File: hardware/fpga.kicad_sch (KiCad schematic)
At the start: 53 parts, among them J10 Conn_01x03_Pin, J11 Conn_01x03_Pin, J12 Conn_01x10_Pin, J14 Conn_01x03_Pin, J15 Conn_01x02_Pin, J16 Conn_01x03_Pin, U1 ICE40HX4K-TQ144, U2 74HC244

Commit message: route mcu
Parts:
- added C149: 100n, Capacitor_SMD:C_0402_1005Metric, symbol Device:C
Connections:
- net +1V2: now also C149.1
- net GND: now also C149.2
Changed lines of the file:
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@@
 	)
 	(junction
+		(at 73.66 133.35)
+		(diameter 0)
+		(color 0 0 0 0)
+	)
+	(junction
 		(at 248.92 24.13)
 		(diameter 0)
@@
 	)
 	(junction
+		(at 68.58 123.19)
+		(diameter 0)
+		(color 0 0 0 0)
+	)
+	(junction
 		(at 93.98 153.67)
 		(diameter 0)
@@
 		)
 	)
+	(wire
+		(pts
+			(xy 68.58 123.19) (xy 68.58 124.46)
+		)
+		(stroke
+			(width 0)
+			(type default)
+		)
+	)
 	(bus
 		(pts
@@
 		)
 	)
+	(wire
+		(pts
+			(xy 68.58 133.35) (xy 73.66 133.35)
+		)
+		(stroke
+			(width 0)
+			(type default)
+		)
+	)
 	(bus
 		(pts
@@
 	(wire
 		(pts
-			(xy 58.42 123.19) (xy 73.66 123.19)
+			(xy 58.42 123.19) (xy 68.58 123.19)
 		)
 		(stroke
@@
 		)
 	)
+	(wire
+		(pts
+			(xy 68.58 123.19) (xy 73.66 123.19)
+		)
+		(stroke
+			(width 0)
+			(type default)
+		)
+	)
 	(bus
 		(pts
@@
 	(wire
 		(pts
+			(xy 68.58 132.08) (xy 68.58 133.35)
+		)
+		(stroke
+			(width 0)
+			(type default)
+		)
+	)
+	(wire
+		(pts
 			(xy 93.98 166.37) (xy 93.98 153.67)
 		)
@@
 					(unit 1)
 				)
+			)
+		)
+	)
+	(symbol
+		(lib_id "Device:C")
+		(at 68.58 128.27 0)
+		(unit 1)
+		(exclude_from_sim no)
+		(in_bom yes)
+		(on_board yes)
+		(dnp no)
+		(property "Reference" "C149"
+			(at 68.58 124.46 0)
+			(effects
+				(font
+					(size 1.27 1.27)
+				)
+				(justify left)
+			)
+		)
+		(property "Value" "100n"
+			(at 68.58 126.2379 0)
+			(effects
+				(font
+					(size 1.27 1.27)
+				)
+				(justify left)
+			)
+		)
+		(property "Footprint" "Capacitor_SMD:C_0402_1005Metric"
+			(at 69.5452 132.08 0)
+			(effects
+				(font
+					(size 1.27 1.27)
+				)
+				(hide yes)
+			)
+		)
+		(property "Datasheet" "~"
+			(at 68.58 128.27 0)
+			(effects
+				(font
+					(size 1.27 1.27)
+				)
+				(hide yes)
+			)
+		)
+		(property "Description" "Unpolarized capacitor"
+			(at 68.58 128.27 0)
+			(effects
+				(font
+					(size 1.27 1.27)
+				)
+				(hide yes)
+			)
+		)
+		(property "LCSC" "C307331"
+			(at 68.58 128.27 0)
+			(effects
+				(font
+					(size 1.27 1.27)
+				)
+				(hide yes)
+			)
+		)
+		(pin "1"
+		)
+		(pin "2"
+		)
+		(instances
+			(project "digital"
+				(path "/4c5c7ce5-09d6-4a32-b2a0-f32b0c47f27d/5a0bf45b-8051-4130-a070-b09b8e450297"
+					(reference "C149")
+					(unit 1)
+				)

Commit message: wire until sipm power
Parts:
- R20: footprint Resistor_SMD:R_0603_1608Metric -> Resistor_SMD:R_0402_1005Metric; LCSC C21189 -> (none)
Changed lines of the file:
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@@
 			)
 		)
-		(property "Footprint" "Resistor_SMD:R_0603_1608Metric"
+		(property "Footprint" "Resistor_SMD:R_0402_1005Metric"
 			(at 90.678 172.72 90)
 			(effects
@@
 			)
 		)
-		(property "LCSC" "C21189"
+		(property "LCSC" ""
 			(at 88.9 172.72 0)
 			(effects

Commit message: route
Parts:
- renumbered C6 to C10, C7 to C11, C149 to C12, C8 to C13, C10 to C14, C11 to C15, C13 to C16, C14 to C17, C15 to C18, C16 to C19, C17 to C20, C18 to C21, C19 to C22, C20 to C23, C148 to C3, C3 to C4, C147 to C5, C4 to C6, C12 to C7, C5 to C8, J14 to J13, J15 to J14, J16 to J15, TP43 to TP1, TP44 to TP2, TP1 to TP3
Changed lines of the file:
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@@
 		(on_board yes)
 		(dnp no)
-		(property "Reference" "C13"
+		(property "Reference" "C16"
 			(at 88.9 124.46 0)
 			(effects
@@
 			(project "digital"
 				(path "/4c5c7ce5-09d6-4a32-b2a0-f32b0c47f27d/5a0bf45b-8051-4130-a070-b09b8e450297"
-					(reference "C13")
+					(reference "C16")
 					(unit 1)
 				)
@@
 		(on_board yes)
 		(dnp no)
-		(property "Reference" "C18"
+		(property "Reference" "C21"
 			(at 80.01 144.78 0)
 			(effects
@@
 			(project "digital"
 				(path "/4c5c7ce5-09d6-4a32-b2a0-f32b0c47f27d/5a0bf45b-8051-4130-a070-b09b8e450297"
-					(reference "C18")
+					(reference "C21")
 					(unit 1)
 				)
@@
 		(on_board yes)
 		(dnp no)
-		(property "Reference" "C10"
+		(property "Reference" "C14"
 			(at 78.74 124.46 0)
 			(effects
@@
 			(project "digital"
 				(path "/4c5c7ce5-09d6-4a32-b2a0-f32b0c47f27d/5a0bf45b-8051-4130-a070-b09b8e450297"
-					(reference "C10")
+					(reference "C14")
 					(unit 1)
 				)
@@
 		(on_board yes)
 		(dnp no)
-		(property "Reference" "C14"
+		(property "Reference" "C17"
 			(at 35.306 129.286 90)
 			(effects
@@
 			(project "digital"
 				(path "/4c5c7ce5-09d6-4a32-b2a0-f32b0c47f27d/5a0bf45b-8051-4130-a070-b09b8e450297"
-					(reference "C14")
+					(reference "C17")
 					(unit 1)
 				)
@@
 		(on_board yes)
 		(dnp no)
-		(property "Reference" "C20"
+		(property "Reference" "C23"
 			(at 93.98 144.78 0)
 			(effects
@@
 			(project "digital"
 				(path "/4c5c7ce5-09d6-4a32-b2a0-f32b0c47f27d/5a0bf45b-8051-4130-a070-b09b8e450297"
-					(reference "C20")
+					(reference "C23")
 					(unit 1)
 				)
@@
 		(on_board yes)
 		(dnp no)
-		(property "Reference" "C147"
+		(property "Reference" "C5"
 			(at 140.97 25.4 0)
 			(effects
@@
 			(project "digital"
 				(path "/4c5c7ce5-09d6-4a32-b2a0-f32b0c47f27d/5a0bf45b-8051-4130-a070-b09b8e450297"
-					(reference "C147")
+					(reference "C5")
 					(unit 1)
 				)
@@
 		(on_board yes)
 		(dnp no)
-		(property "Reference" "TP1"
+		(property "Reference" "TP3"
 			(at 41.402 109.982 90)
 			(effects
@@
 			(project "digital"
 				(path "/4c5c7ce5-09d6-4a32-b2a0-f32b0c47f27d/5a0bf45b-8051-4130-a070-b09b8e450297"
-					(reference "TP1")
+					(reference "TP3")
 					(unit 1)
 				)
@@
 		(on_board yes)
 		(dnp no)
-		(property "Reference" "C8"
+		(property "Reference" "C13"
 			(at 73.66 124.46 0)
 			(effects
@@
 			(project "digital"
 				(path "/4c5c7ce5-09d6-4a32-b2a0-f32b0c47f27d/5a0bf45b-8051-4130-a070-b09b8e450297"
-					(reference "C8")
+					(reference "C13")
 					(unit 1)
 				)
@@
 		(on_board yes)
 		(dnp no)
-		(property "Reference" "J16"
+		(property "Reference" "J15"
 			(at 96.266 90.678 0)
 			(effects
@@
 			(project "digital"
 				(path "/4c5c7ce5-09d6-4a32-b2a0-f32b0c47f27d/5a0bf45b-8051-4130-a070-b09b8e450297"
-					(reference "J16")
+					(reference "J15")
 					(unit 1)
 				)
@@
 		(on_board yes)
 		(dnp no)
-		(property "Reference" "C15"
+		(property "Reference" "C18"
 			(at 35.306 134.366 90)
 			(effects
@@
 			(project "digital"
 				(path "/4c5c7ce5-09d6-4a32-b2a0-f32b0c47f27d/5a0bf45b-8051-4130-a070-b09b8e450297"
-					(reference "C15")
+					(reference "C18")
 					(unit 1)
 				)
@@
 		(on_board yes)
 		(dnp no)
-		(property "Reference" "C11"
+		(property "Reference" "C15"
 			(at 83.82 124.46 0)
 			(effects
@@
 			(project "digital"
 				(path "/4c5c7ce5-09d6-4a32-b2a0-f32b0c47f27d/5a0bf45b-8051-4130-a070-b09b8e450297"
-					(reference "C11")
+					(reference "C15")
 					(unit 1)
 				)
@@
 		(on_board yes)
 		(dnp no)
-		(property "Reference" "C7"
+		(property "Reference" "C11"
 			(at 158.496 110.236 90)
 			(effects
@@
 			(project "digital"
 				(path "/4c5c7ce5-09d6-4a32-b2a0-f32b0c47f27d/5a0bf45b-8051-4130-a070-b09b8e450297"
-					(reference "C7")
+					(reference "C11")
 					(unit 1)
 				)
@@
 		(on_board yes)
 		(dnp no)
-		(property "Reference" "C3"
+		(property "Reference" "C4"
 			(at 135.89 25.4 0)
 			(effects
@@
 			(project "digital"
 				(path "/4c5c7ce5-09d6-4a32-b2a0-f32b0c47f27d/5a0bf45b-8051-4130-a070-b09b8e450297"
-					(reference "C3")
+					(reference "C4")
 					(unit 1)
 				)
@@
 		(on_board yes)
 		(dnp no)
-		(property "Reference" "J15"
+		(property "Reference" "J14"
 			(at 222.25 82.2959 0)
 			(effects
@@
 			(project "digital"
 				(path "/4c5c7ce5-09d6-4a32-b2a0-f32b0c47f27d/5a0bf45b-8051-4130-a070-b09b8e450297"
-					(reference "J15")
+					(reference "J14")
 					(unit 1)
 				)
@@
 		(on_board yes)
 		(dnp no)
-		(property "Reference" "C149"
+		(property "Reference" "C12"
 			(at 68.58 124.46 0)
 			(effects
@@
 			(project "digital"
 				(path "/4c5c7ce5-09d6-4a32-b2a0-f32b0c47f27d/5a0bf45b-8051-4130-a070-b09b8e450297"
-					(reference "C149")
+					(reference "C12")
 					(unit 1)
 				)
@@
 		(on_board yes)
 		(dnp no)
-		(property "Reference" "J14"
+		(property "Reference" "J13"
 			(at 153.416 80.518 0)
 			(effects
@@
 			(project "digital"
 				(path "/4c5c7ce5-09d6-4a32-b2a0-f32b0c47f27d/5a0bf45b-8051-4130-a070-b09b8e450297"
-					(reference "J14")
+					(reference "J13")
 					(unit 1)
 				)
@@
 		(on_board yes)
 		(dnp no)
-		(property "Reference" "C5"
+		(property "Reference" "C8"
 			(at 259.08 25.4 0)
 			(effects
@@
 			(project "digital"
 				(path "/4c5c7ce5-09d6-4a32-b2a0-f32b0c47f27d/5a0bf45b-8051-4130-a070-b09b8e450297"
-					(reference "C5")
+					(reference "C8")
 					(unit 1)
 				)
@@
 		(on_board yes)
 		(dnp no)
-		(property "Reference" "C19"
+		(property "Reference" "C22"
 			(at 85.09 144.78 0)
 			(effects
@@
 			(project "digital"
 				(path "/4c5c7ce5-09d6-4a32-b2a0-f32b0c47f27d/5a0bf45b-8051-4130-a070-b09b8e450297"
-					(reference "C19")
+					(reference "C22")
 					(unit 1)
 				)
@@
 		(on_board yes)
 		(dnp no)
-		(property "Reference" "TP43"
+		(property "Reference" "TP1"
 			(at 30.48 80.01 90)
 			(effects
@@
 			(project "digital"
 				(path "/4c5c7ce5-09d6-4a32-b2a0-f32b0c47f27d/5a0bf45b-8051-4130-a070-b09b8e450297"
-					(reference "TP43")
+					(reference "TP1")
 					(unit 1)
 				)
@@
 		(on_board yes)
 		(dnp no)
-		(property "Reference" "C4"
+		(property "Reference" "C6"
 			(at 193.04 25.4 0)
 			(effects
@@
 			(project "digital"
 				(path "/4c5c7ce5-09d6-4a32-b2a0-f32b0c47f27d/5a0bf45b-8051-4130-a070-b09b8e450297"
-					(reference "C4")
+					(reference "C6")
 					(unit 1)
 				)
@@
 		(on_board yes)
 		(dnp no)
-		(property "Reference" "TP44"
+		(property "Reference" "TP2"
 			(at 30.48 82.55 90)
 			(effects
@@
 			(project "digital"
 				(path "/4c5c7ce5-09d6-4a32-b2a0-f32b0c47f27d/5a0bf45b-8051-4130-a070-b09b8e450297"
-					(reference "TP44")
+					(reference "TP2")
 					(unit 1)
 				)
@@
 		(on_board yes)
 		(dnp no)
-		(property "Reference" "C12"
+		(property "Reference" "C7"
 			(at 198.12 25.4 0)
 			(effects
@@
 			(project "digital"
 				(path "/4c5c7ce5-09d6-4a32-b2a0-f32b0c47f27d/5a0bf45b-8051-4130-a070-b09b8e450297"
-					(reference "C12")
+					(reference "C7")
 					(unit 1)
 				)
@@
 		(on_board yes)
 		(dnp no)
-		(property "Reference" "C148"
+		(property "Reference" "C3"
 			(at 85.09 25.4 0)
 			(effects
@@
 			(project "digital"
 				(path "/4c5c7ce5-09d6-4a32-b2a0-f32b0c47f27d/5a0bf45b-8051-4130-a070-b09b8e450297"
-					(reference "C148")
+					(reference "C3")
 					(unit 1)
 				)
@@
 		(on_board yes)
 		(dnp no)
-		(property "Reference" "C6"
+		(property "Reference" "C10"
 			(at 156.21 105.664 90)
 			(effects
@@
 			(project "digital"
 				(path "/4c5c7ce5-09d6-4a32-b2a0-f32b0c47f27d/5a0bf45b-8051-4130-a070-b09b8e450297"
-					(reference "C6")
+					(reference "C10")
 					(unit 1)
 				)
@@
 		(on_board yes)
 		(dnp no)
-		(property "Reference" "C17"
+		(property "Reference" "C20"
 			(at 35.306 144.526 90)
 			(effects
@@
 			(project "digital"
 				(path "/4c5c7ce5-09d6-4a32-b2a0-f32b0c47f27d/5a0bf45b-8051-4130-a070-b09b8e450297"
-					(reference "C17")
+					(reference "C20")
 					(unit 1)
 				)
@@
 		(on_board yes)
 		(dnp no)
-		(property "Reference" "C16"
+		(property "Reference" "C19"
 			(at 35.306 139.446 90)
 			(effects
@@
 			(project "digital"
 				(path "/4c5c7ce5-09d6-4a32-b2a0-f32b0c47f27d/5a0bf45b-8051-4130-a070-b09b8e450297"
-					(reference "C16")
+					(reference "C19")
 					(unit 1)
 				)

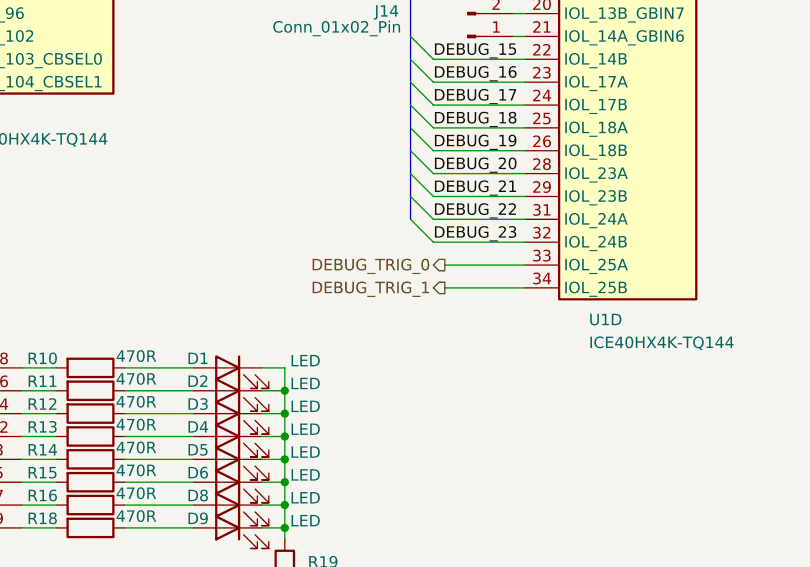
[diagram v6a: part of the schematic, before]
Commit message: route all signal
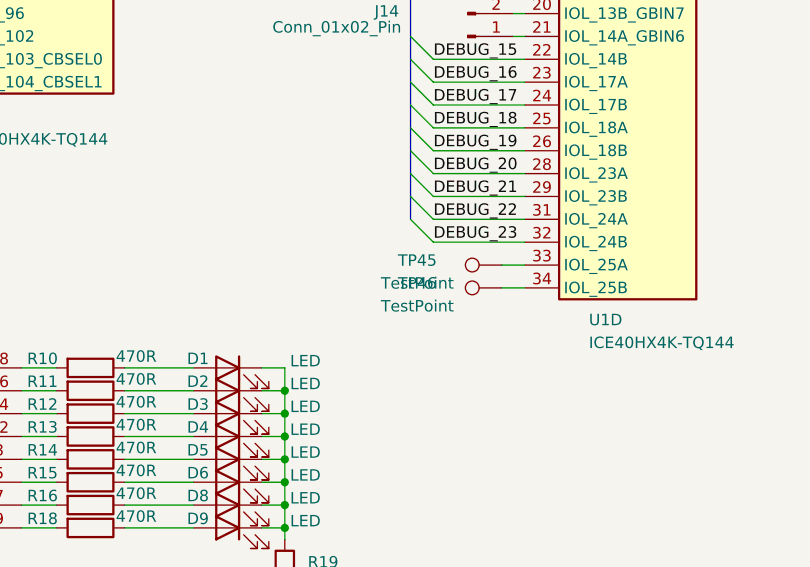
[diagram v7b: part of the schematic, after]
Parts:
- added TP45, TP46: TestPoint, TestPoint:TestPoint_Pad_D1.0mm, symbol Connector:TestPoint
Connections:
- net DEBUG_TRIG_0: no longer names the net of U1.33 (IOL_25A)
- net DEBUG_TRIG_0: now also TP45.1
- net DEBUG_TRIG_1: no longer names the net of U1.34 (IOL_25B)
- net DEBUG_TRIG_1: now also TP46.1
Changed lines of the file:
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@@
 	(wire
 		(pts
+			(xy 233.68 110.49) (xy 236.22 110.49)
+		)
+		(stroke
+			(width 0)
+			(type default)
+		)
+	)
+	(wire
+		(pts
 			(xy 259.08 34.29) (xy 259.08 35.56)
 		)
@@
 	(wire
 		(pts
-			(xy 227.33 113.03) (xy 236.22 113.03)
-		)
-		(stroke
-			(width 0)
-			(type default)
-		)
-	)
-	(wire
-		(pts
 			(xy 76.2 165.1) (xy 78.74 165.1)
 		)
@@
 		)
 	)
+	(wire
+		(pts
+			(xy 233.68 113.03) (xy 236.22 113.03)
+		)
+		(stroke
+			(width 0)
+			(type default)
+		)
+	)
 	(bus
 		(pts
@@
 	(wire
 		(pts
-			(xy 227.33 110.49) (xy 236.22 110.49)
-		)
-		(stroke
-			(width 0)
-			(type default)
-		)
-	)
-	(wire
-		(pts
 			(xy 259.08 24.13) (xy 248.92 24.13)
 		)
@@
 		)
 	)
-	(hierarchical_label "DEBUG_TRIG_1"
-		(shape output)
-		(at 227.33 113.03 180)
-		(effects
-			(font
-				(size 1.27 1.27)
-			)
-			(justify right)
-		)
-	)
 	(hierarchical_label "CDONE"
 		(shape output)
@@
 		)
 	)
-	(hierarchical_label "DEBUG_TRIG_0"
-		(shape output)
-		(at 227.33 110.49 180)
-		(effects
-			(font
-				(size 1.27 1.27)
-			)
-			(justify right)
-		)
-	)
 	(symbol
 		(lib_id "Device:R")
@@
 	)
 	(symbol
+		(lib_id "Connector:TestPoint")
+		(at 233.68 110.49 90)
+		(mirror x)
+		(unit 1)
+		(exclude_from_sim no)
+		(in_bom yes)
+		(on_board yes)
+		(dnp no)
+		(property "Reference" "TP45"
+			(at 224.282 109.982 90)
+			(effects
+				(font
+					(size 1.27 1.27)
+				)
+			)
+		)
+		(property "Value" "TestPoint"
+			(at 224.282 112.522 90)
+			(effects
+				(font
+					(size 1.27 1.27)
+				)
+			)
+		)
+		(property "Footprint" "TestPoint:TestPoint_Pad_D1.0mm"
+			(at 233.68 115.57 0)
+			(effects
+				(font
+					(size 1.27 1.27)
+				)
+				(hide yes)
+			)
+		)
+		(property "Datasheet" "~"
+			(at 233.68 115.57 0)
+			(effects
+				(font
+					(size 1.27 1.27)
+				)
+				(hide yes)
+			)
+		)
+		(property "Description" "test point"
+			(at 233.68 110.49 0)
+			(effects
+				(font
+					(size 1.27 1.27)
+				)
+				(hide yes)
+			)
+		)
+		(pin "1"
+		)
+		(instances
+			(project "digital"
+				(path "/4c5c7ce5-09d6-4a32-b2a0-f32b0c47f27d/5a0bf45b-8051-4130-a070-b09b8e450297"
+					(reference "TP45")
+					(unit 1)
+				)
+			)
+		)
+	)
+	(symbol
 		(lib_id "Device:R")
 		(at 187.96 121.92 270)
@@
 					(unit 1)
 				)
+			)
+		)
+	)
+	(symbol
+		(lib_id "Connector:TestPoint")
+		(at 233.68 113.03 90)
+		(mirror x)
+		(unit 1)
+		(exclude_from_sim no)
+		(in_bom yes)
+		(on_board yes)
+		(dnp no)
+		(property "Reference" "TP46"
+			(at 224.282 112.522 90)
+			(effects
+				(font
+					(size 1.27 1.27)
+				)
+			)
+		)
+		(property "Value" "TestPoint"
+			(at 224.282 115.062 90)
+			(effects
+				(font
+					(size 1.27 1.27)
+				)
+			)
+		)
+		(property "Footprint" "TestPoint:TestPoint_Pad_D1.0mm"
+			(at 233.68 118.11 0)
+			(effects
+				(font
+					(size 1.27 1.27)
+				)
+				(hide yes)
+			)
+		)
+		(property "Datasheet" "~"
+			(at 233.68 118.11 0)
+			(effects
+				(font
+					(size 1.27 1.27)
+				)
+				(hide yes)
+			)
+		)
+		(property "Description" "test point"
+			(at 233.68 113.03 0)
+			(effects
+				(font
+					(size 1.27 1.27)
+				)
+				(hide yes)
+			)
+		)
+		(pin "1"
+		)
+		(instances
+			(project "digital"
+				(path "/4c5c7ce5-09d6-4a32-b2a0-f32b0c47f27d/5a0bf45b-8051-4130-a070-b09b8e450297"
+					(reference "TP46")
+					(unit 1)
+				)
